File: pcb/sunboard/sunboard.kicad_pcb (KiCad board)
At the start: 2 copper layers, 311 parts, among them SW1 SW_Push, SW10 SW_Push, SW100 SW_Push, SW101 SW_Push, SW102 SW_Push, SW103 SW_Push, SW104 SW_Push, SW105 SW_Push, SW106 SW_Push, SW107 SW_Push, SW108 SW_Push, SW109 SW_Push, SW11 SW_Push, SW110 SW_Push, SW111 SW_Push, SW112 SW_Push, SW113 SW_Push, SW114 SW_Push, SW115 SW_Push, SW116 SW_Push, SW117 SW_Push, SW118 SW_Push, SW119 SW_Push, SW12 SW_Push, SW120 SW_Push, SW121 SW_Push, SW122 SW_Push, SW123 SW_Push, SW124 SW_Push, SW125 SW_Push, SW126 SW_Push, SW127 SW_Push, SW128 SW_Push, SW129 SW_Push, SW13 SW_Push, SW130 SW_Push, SW131 SW_Push, SW132 SW_Push, SW133 SW_Push, SW134 SW_Push, SW135 SW_Push, SW136 SW_Push, SW137 SW_Push, SW138 SW_Push, SW139 SW_Push, SW14 SW_Push, SW140 SW_Push, SW141 SW_Push, SW142 SW_Push, SW143 SW_Push, SW144 SW_Push, SW145 SW_Push, SW146 SW_Push, SW147 SW_Push, SW148 SW_Push, SW149 SW_Push, SW15 SW_Push, SW150 SW_Push, SW151 SW_Push, SW152 SW_Push, SW153 SW_Push, SW154 SW_Push, SW16 SW_Push, SW17 SW_Push, SW18 SW_Push, SW19 SW_Push, SW2 SW_Push, SW20 SW_Push, SW21 SW_Push, SW22 SW_Push, SW23 SW_Push, SW24 SW_Push, SW25 SW_Push, SW26 SW_Push, SW27 SW_Push, SW28 SW_Push, SW29 SW_Push, SW3 SW_Push, SW30 SW_Push, SW31 SW_Push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

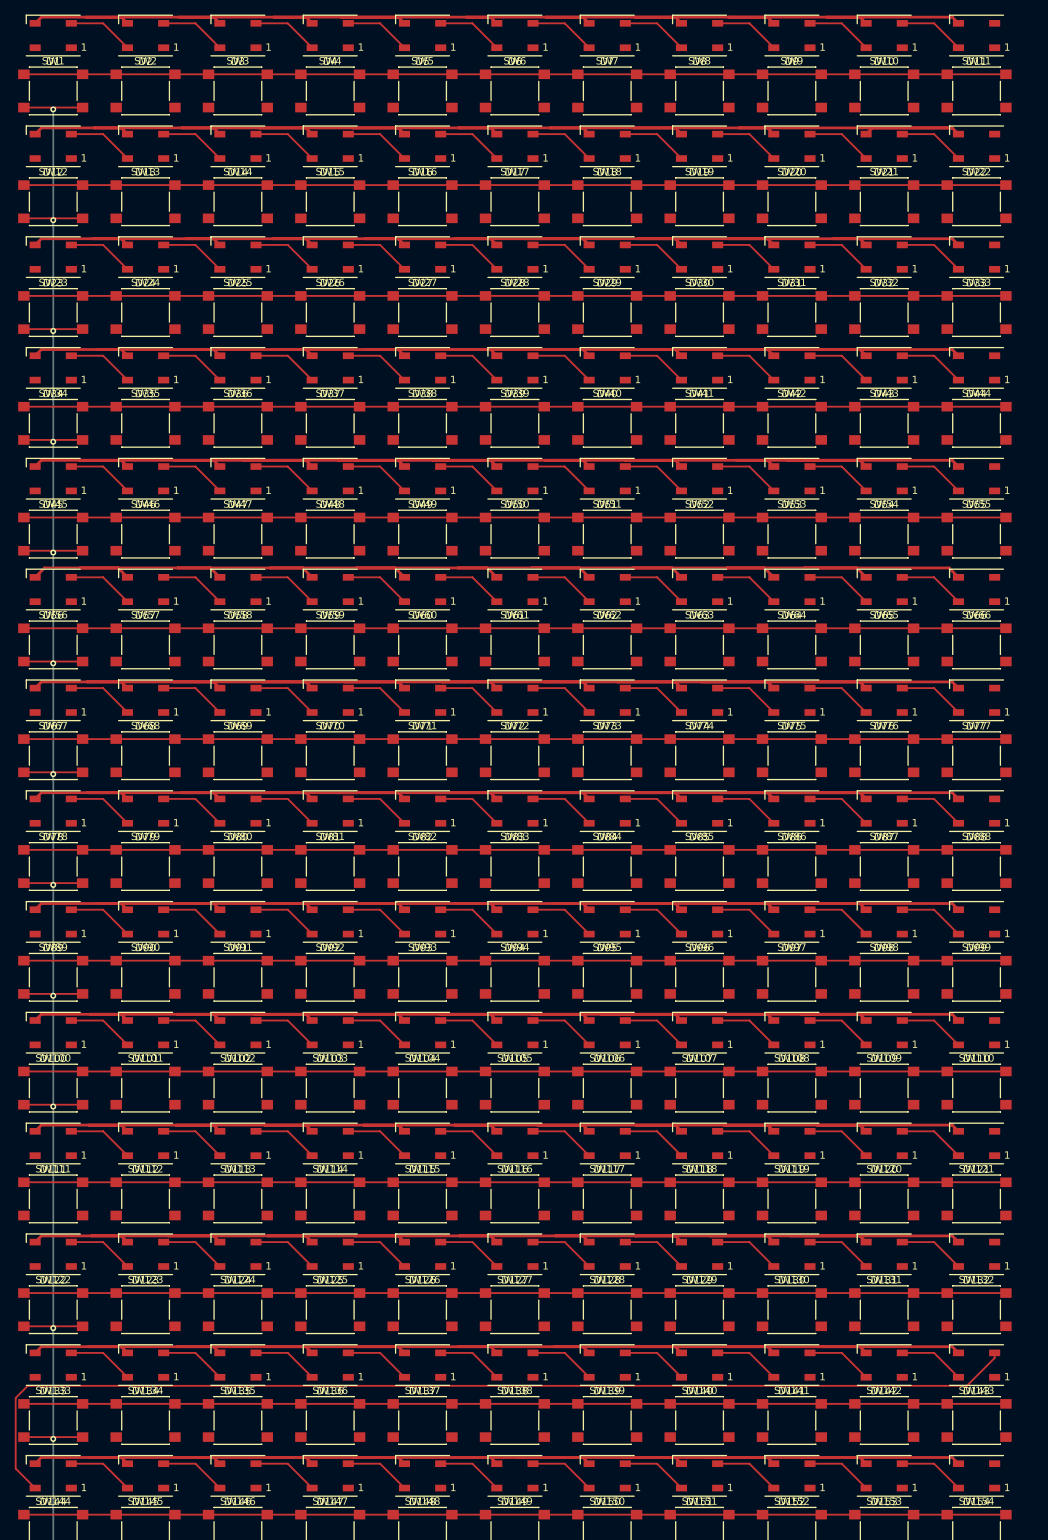
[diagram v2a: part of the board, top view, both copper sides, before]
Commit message: fea(pcb): route vcc
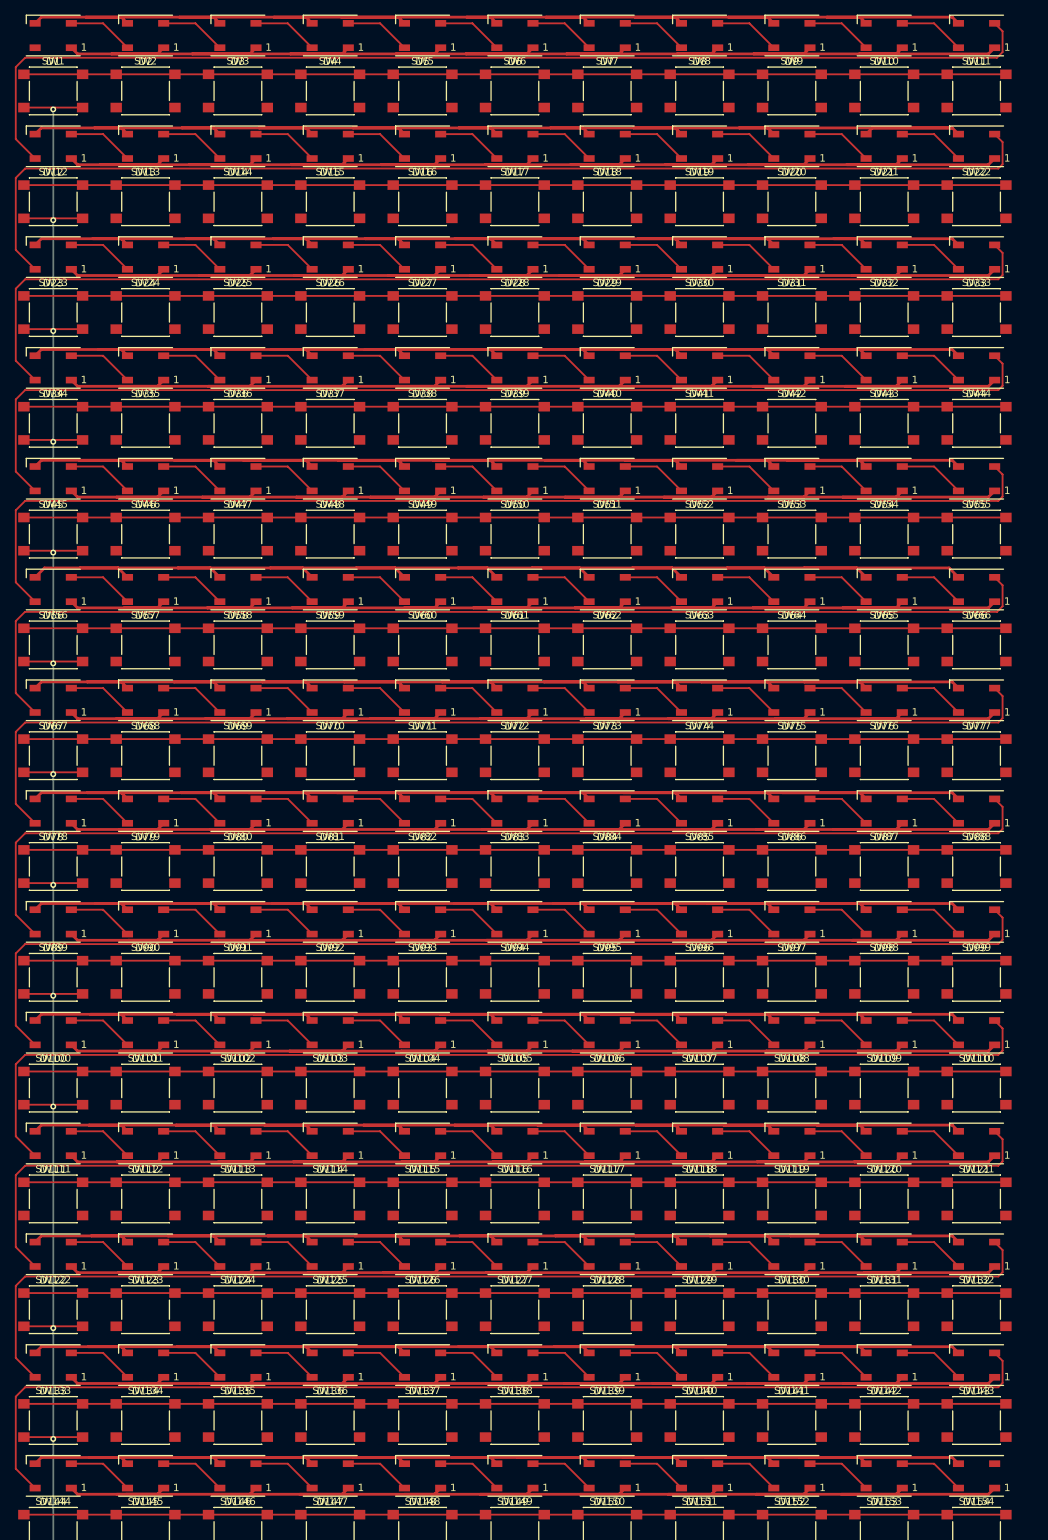
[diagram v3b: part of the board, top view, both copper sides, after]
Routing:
- net +5V: track 0.00 -> 2646.1 mm
- net Net-(D88-DOUT): track 0.00 -> 152.3 mm
- net Net-(D77-DOUT): track 0.00 -> 152.3 mm
- net Net-(D22-DOUT): track 0.00 -> 152.3 mm
- net Net-(D55-DOUT): track 0.00 -> 152.3 mm
- net Net-(D44-DOUT): track 0.00 -> 152.3 mm
- net Net-(D132-DOUT): track 0.00 -> 152.3 mm
- net Net-(D121-DOUT): track 0.00 -> 152.3 mm
- net Net-(D110-DOUT): track 0.00 -> 152.3 mm
- net Net-(D100-DIN): track 0.00 -> 152.3 mm
- net Net-(D33-DOUT): track 0.00 -> 152.3 mm
- net Net-(D66-DOUT): track 0.00 -> 152.3 mm
- net Net-(D11-DOUT): track 0.00 -> 152.2 mm
- net Net-(D143-DOUT): track 148.8 -> 152.3 mm

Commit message: feat(pcb): finish routing main
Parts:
- moved U1 76.9 mm to (205.2, 33.6)
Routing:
- net +5V: track 2646.1 -> 3047.1 mm
- net GND: track 2645.5 -> 3029.7 mm
- net Col4: track 0.00 -> 309.2 mm, vias 0 -> 14
- net Col3: track 0.00 -> 309.2 mm, vias 0 -> 14
- net Col2: track 0.00 -> 309.2 mm, vias 0 -> 14
- net Col9: track 0.00 -> 309.2 mm, vias 0 -> 14
- net Col8: track 0.00 -> 309.2 mm, vias 0 -> 14
- net Col7: track 0.00 -> 309.2 mm, vias 0 -> 14
- net Col6: track 0.00 -> 309.2 mm, vias 0 -> 14
- net Col5: track 0.00 -> 309.2 mm, vias 0 -> 14
- net Col11: track 0.00 -> 309.2 mm, vias 0 -> 14
- net Col10: track 0.00 -> 309.2 mm, vias 0 -> 14
- net Col1: track 301.0 -> 309.2 mm, vias 13 -> 14

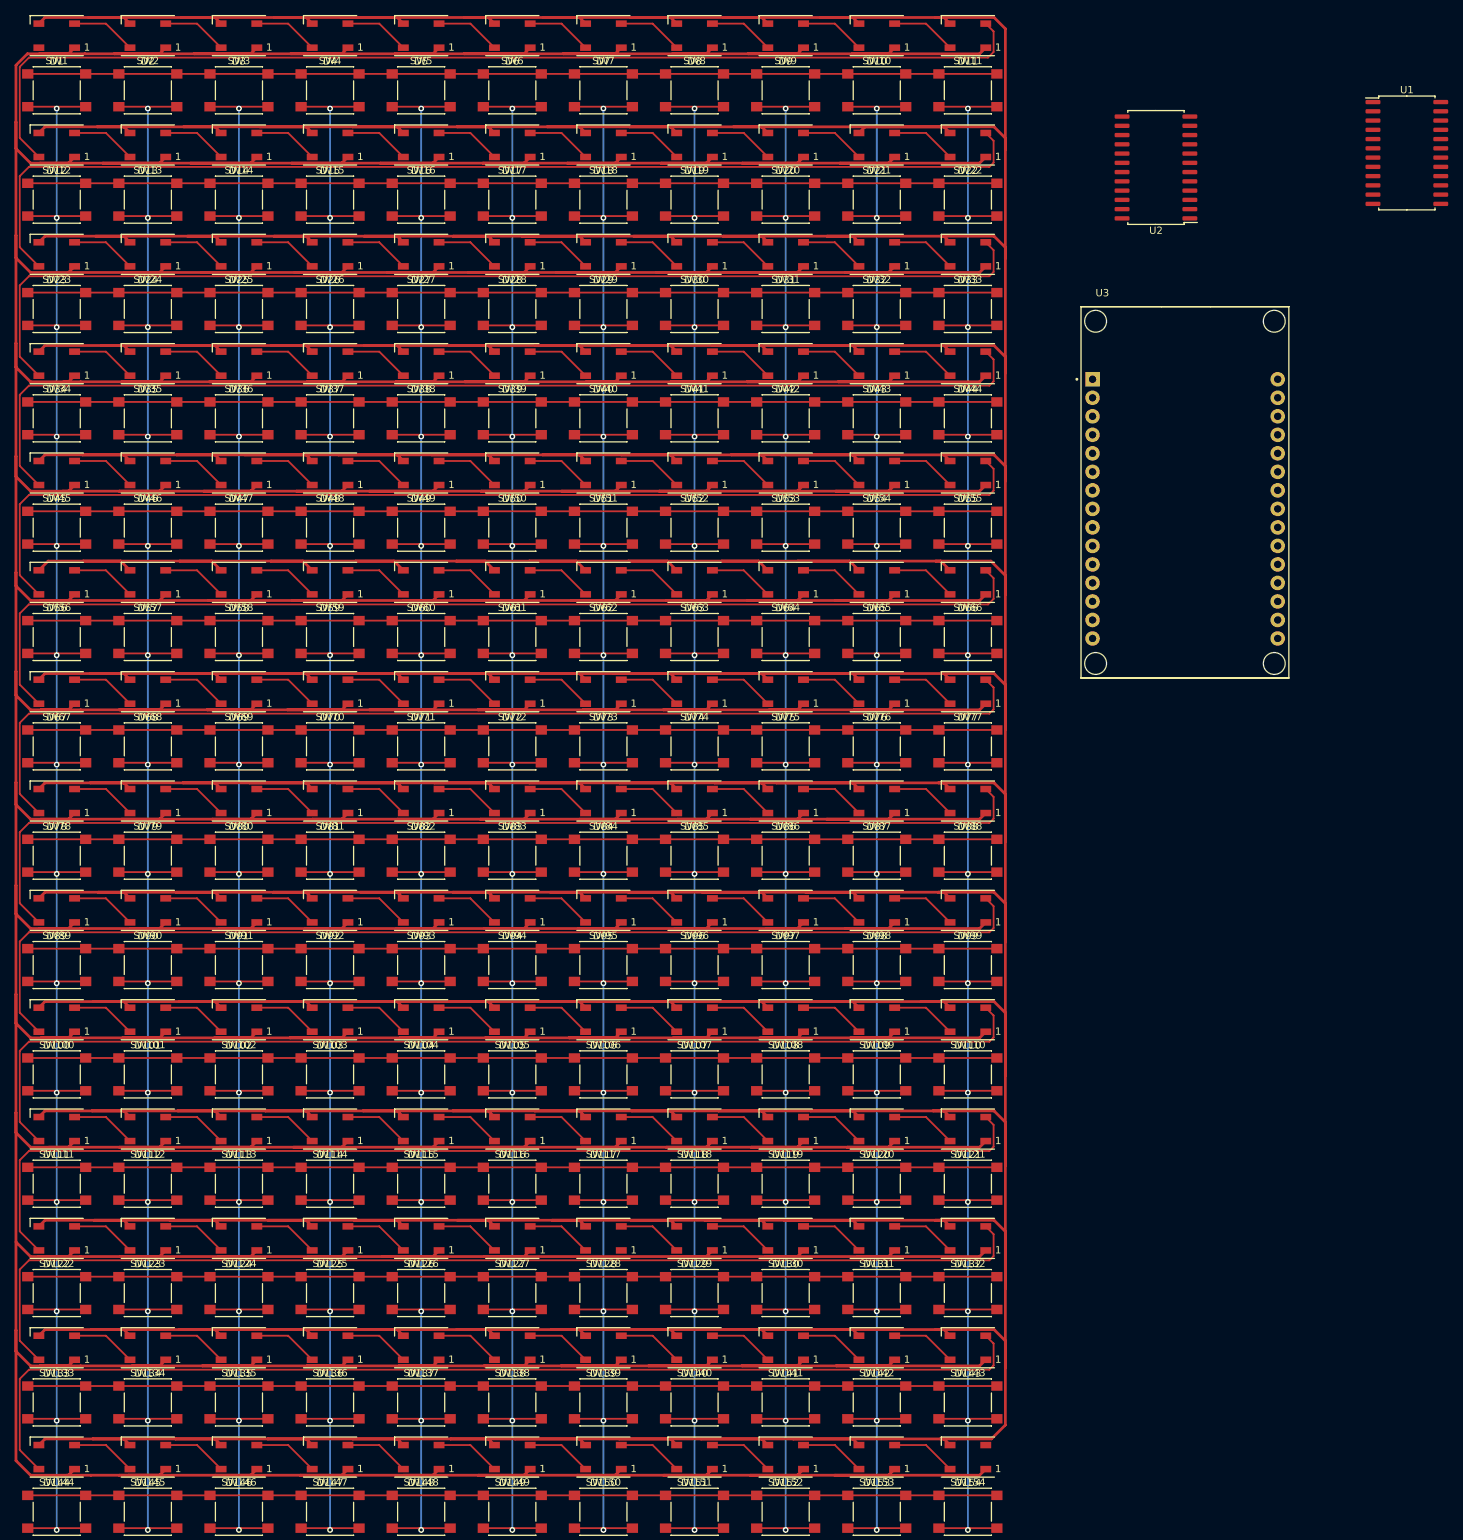
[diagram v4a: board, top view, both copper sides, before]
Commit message: feat(pcb): finish routing main pcb
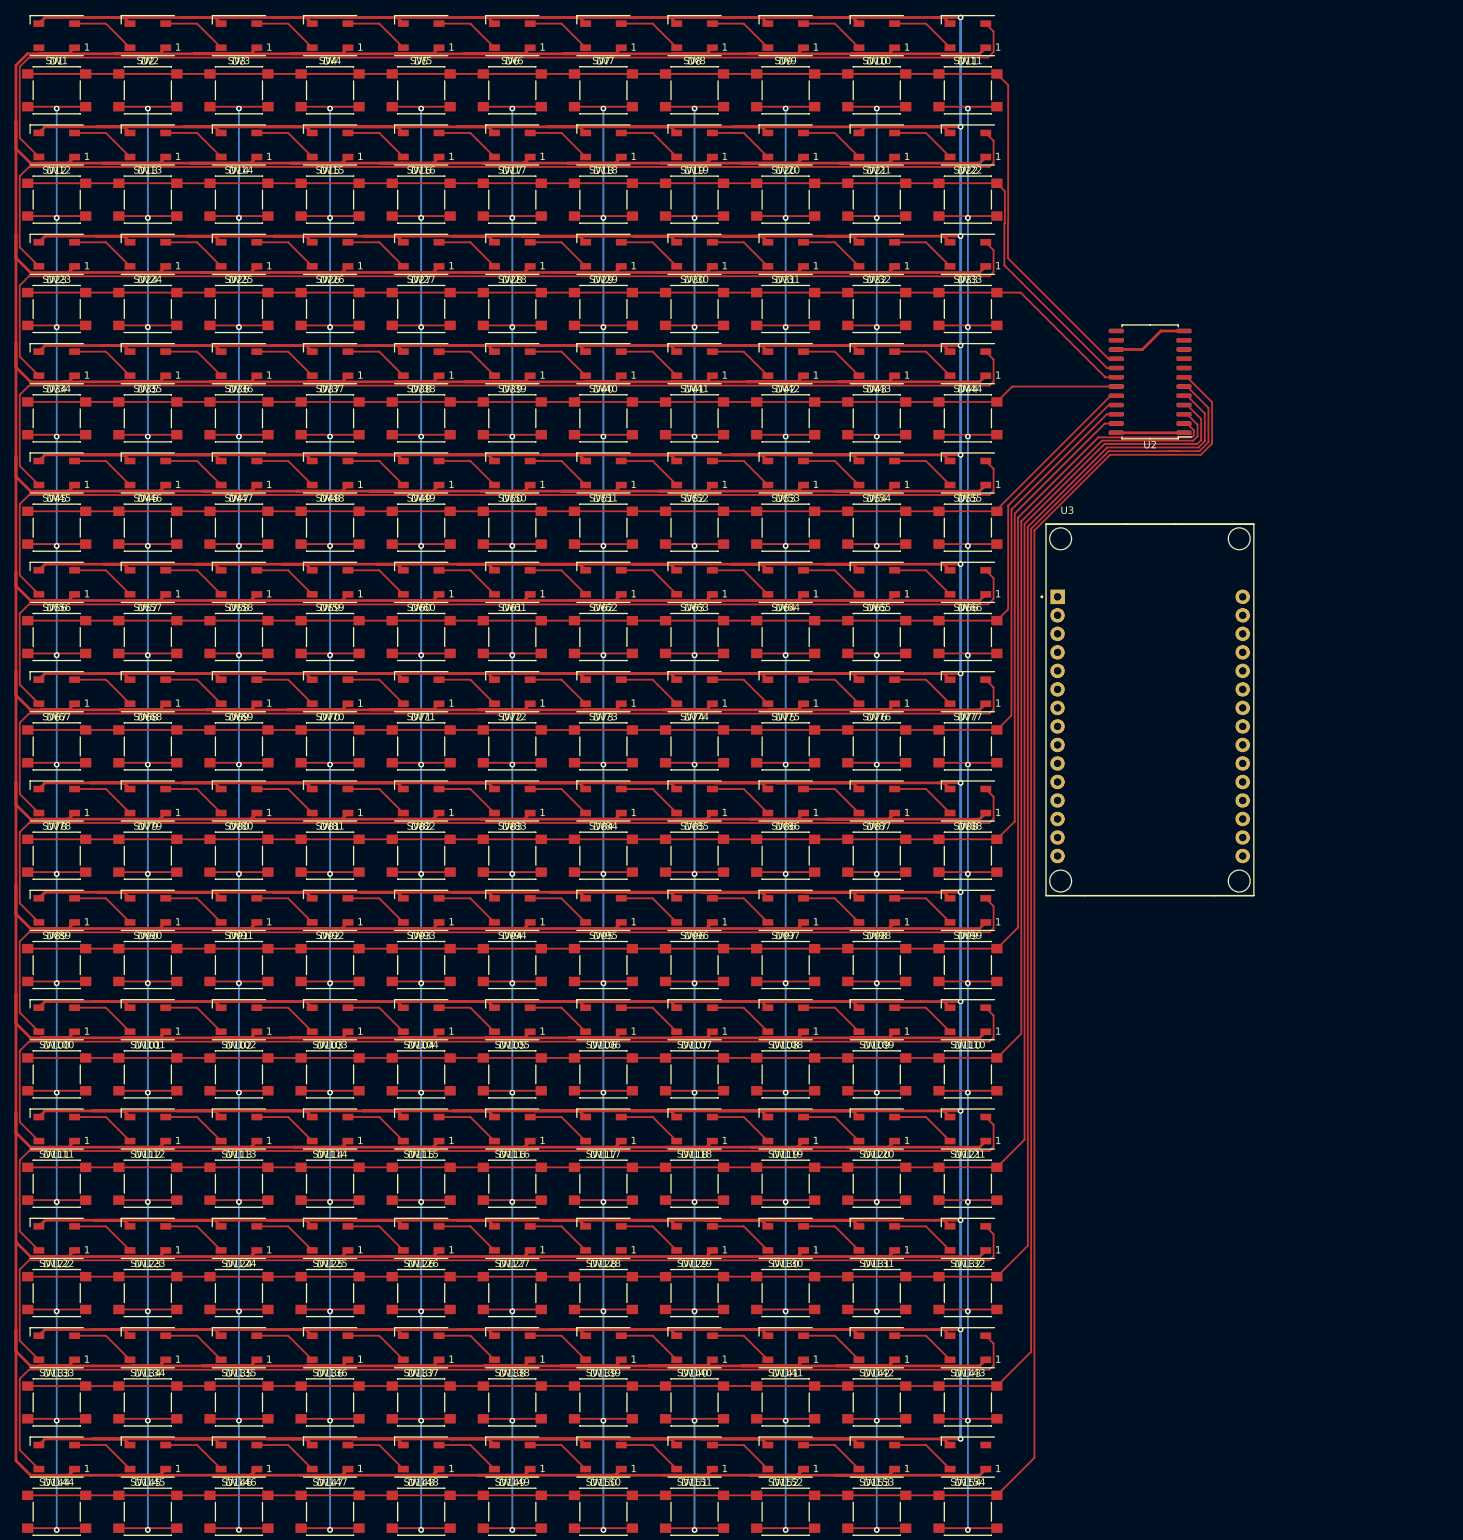
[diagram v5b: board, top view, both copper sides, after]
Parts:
- U1: moved to B.Cu
- moved U1 47.2 mm to (170.0, 65.0), turned to 180 degrees
- moved U3 30.2 mm to (170.0, 110.0)
- moved U2 29.4 mm to (170.0, 65.0)
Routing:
- net Row5: track 132.9 -> 307.7 mm
- net GND: track 3029.7 -> 2865.4 mm, vias 0 -> 14
- net Row6: track 132.9 -> 292.5 mm
- net Row7: track 132.9 -> 274.4 mm
- net Row8: track 132.9 -> 257.8 mm
- net Row9: track 132.9 -> 241.0 mm
- net Row10: track 132.9 -> 224.5 mm
- net Row11: track 132.9 -> 197.7 mm
- net Row12: track 132.9 -> 183.8 mm
- net Row18: track 132.9 -> 179.4 mm
- net Row13: track 132.9 -> 169.9 mm
- net Row17: track 132.9 -> 165.9 mm
- net Row14: track 132.9 -> 156.0 mm
- net Row16: track 132.9 -> 154.1 mm
- net Row15: track 132.9 -> 150.2 mm
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
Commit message: feat(pcb): finish routing pcb
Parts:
- moved U1 88.5 mm to (170.0, 153.5), turned to 0 degrees
- turned U2 to 0 degrees
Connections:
- U1 pad 10: C_SEL1 -> C_SEL3
- U1 pad 11: C_SEL2 -> C_SEL4
- U1 pad 13: C_SEL4 -> C_SEL2
- U1 pad 14: C_SEL3 -> C_SEL1
- U1 pad 2: Col8 -> Col4
- U1 pad 21: Col11 -> Col1
- U1 pad 22: Col10 -> Col2
- U1 pad 23: Col9 -> Col3
- U1 pad 3: Col7 -> Col5
- U1 pad 5: Col5 -> Col7
- U1 pad 6: Col4 -> Col8
- U1 pad 7: Col3 -> Col9
- U1 pad 8: Col2 -> Col10
- U1 pad 9: Col1 -> Col11
- U3 pad 10: C_SEL2 -> STATE
- U3 pad 11: C_SEL3 -> C_SEL4
- U3 pad 14: C_SEL4 -> C_SEL3
- U3 pad 26: STATE -> C_SEL1
- U3 pad 9: C_SEL1 -> C_SEL2
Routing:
- net LED_IN: track 0.00 -> 252.3 mm, vias 0 -> 2
- net Col1: track 309.2 -> 522.9 mm
- net Col2: track 309.2 -> 507.7 mm
- net Col3: track 309.2 -> 492.8 mm
- net Col4: track 309.2 -> 474.6 mm
- net Col5: track 309.2 -> 462.6 mm
- net Col6: track 309.2 -> 450.6 mm
- net VCC: track 9.30 -> 141.4 mm, vias 0 -> 2
- net Col7: track 309.2 -> 438.6 mm
- net Col8: track 309.2 -> 426.7 mm
- net GND: track 2865.4 -> 2979.0 mm, vias 14 -> 18
- net Col9: track 309.2 -> 414.6 mm
- net Col10: track 309.2 -> 402.6 mm
- net Col11: track 309.2 -> 378.2 mm
- net R_SEL4: track 0.00 -> 68.9 mm, vias 0 -> 2
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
